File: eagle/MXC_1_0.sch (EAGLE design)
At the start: 13 parts, among them IC1 74HC93N, X1 Ctrl, X2 Out X

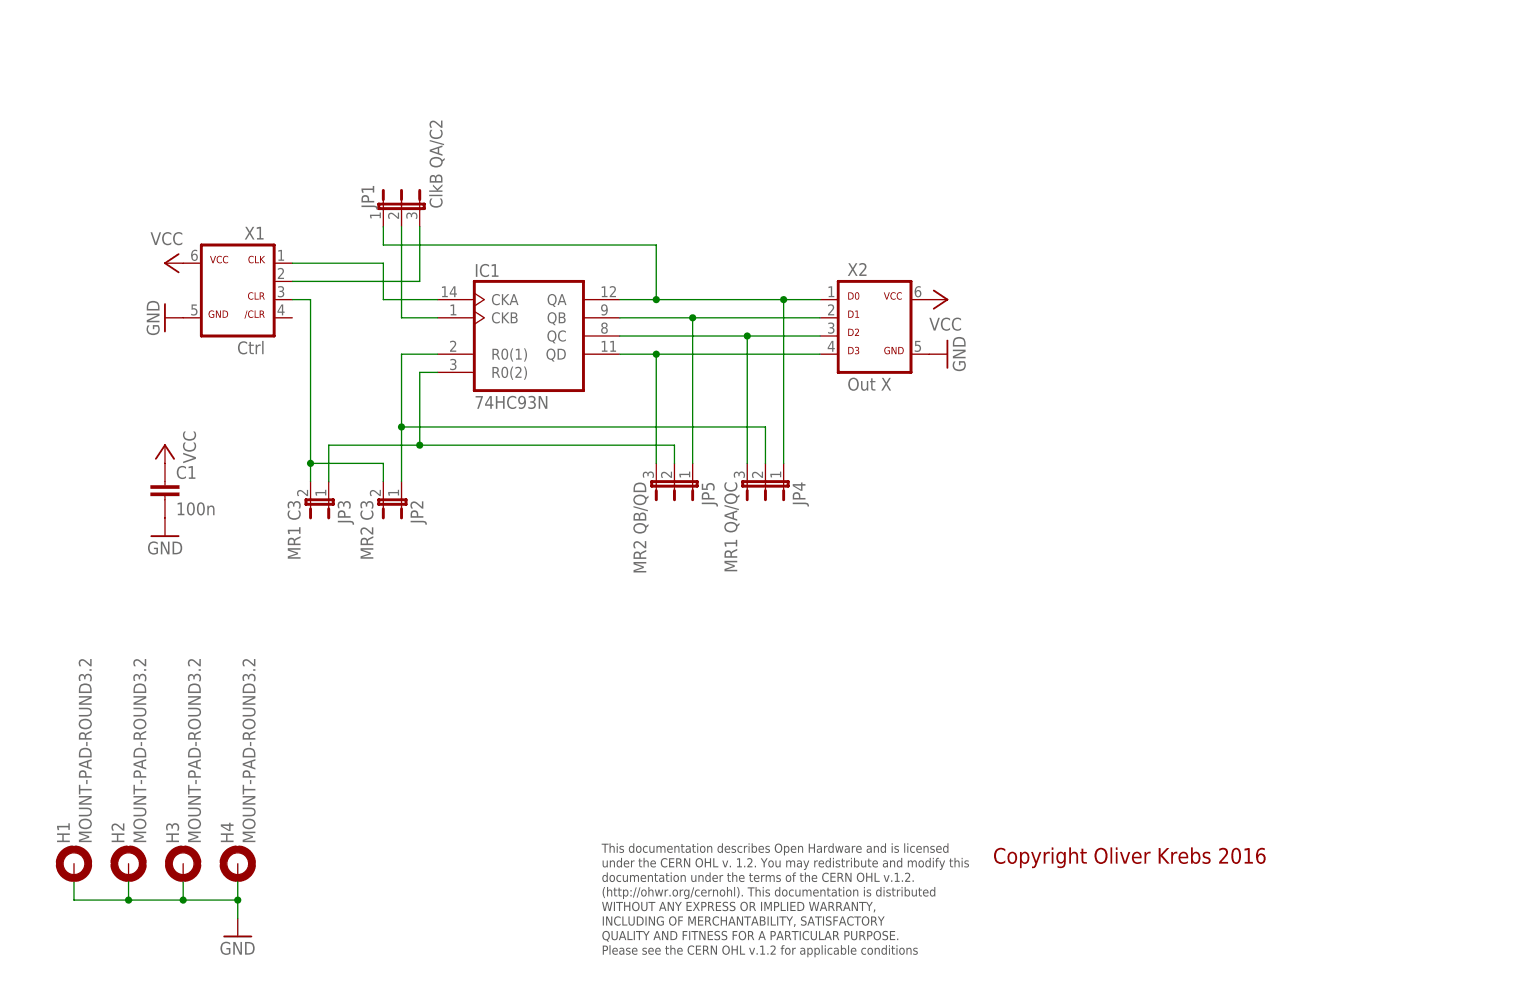
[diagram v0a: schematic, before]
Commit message: Add new tetra-Board and arduino files
Add AMP_1_0, AVC_1_0, D18_1_1, IOP_1_2, MIC_1_0, PIN_1_1, POT_1_0, PWA_1_0, PWR_1_0, RGF 2.0, SOC_2_0, VLT_1_0
Add mex_nano_shield_keyboard, mex_nano_shied_numbers

New arduino projects
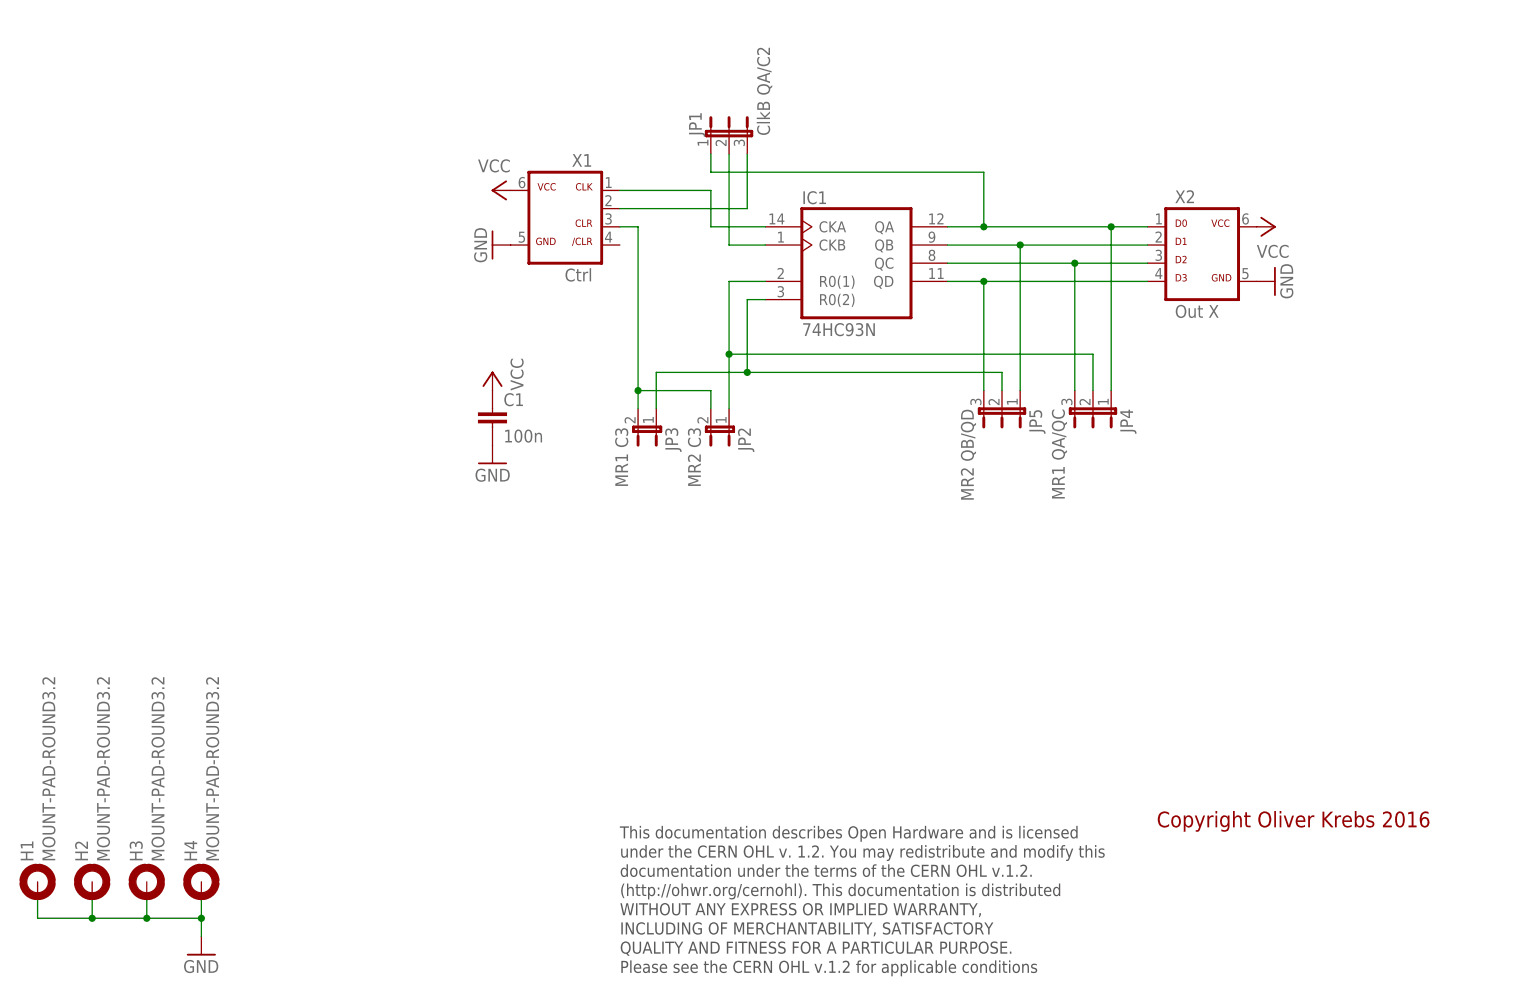
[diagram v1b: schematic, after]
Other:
- moved on the sheet: C1, H1, H2, H3, H4, IC1, JP1, JP2, JP3, JP4, JP5, X1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
